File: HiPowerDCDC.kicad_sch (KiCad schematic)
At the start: 67 parts, among them J1 Conn_01x01, J2 Conn_01x01, J3 Conn_01x01, J4 Conn_01x01, J5 Conn_01x04, Q1 WMJ38N60, Q2 WMJ38N60, SW1 SW_Push, SW2 SW_Push, U1 ESP32-WROOM-32U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

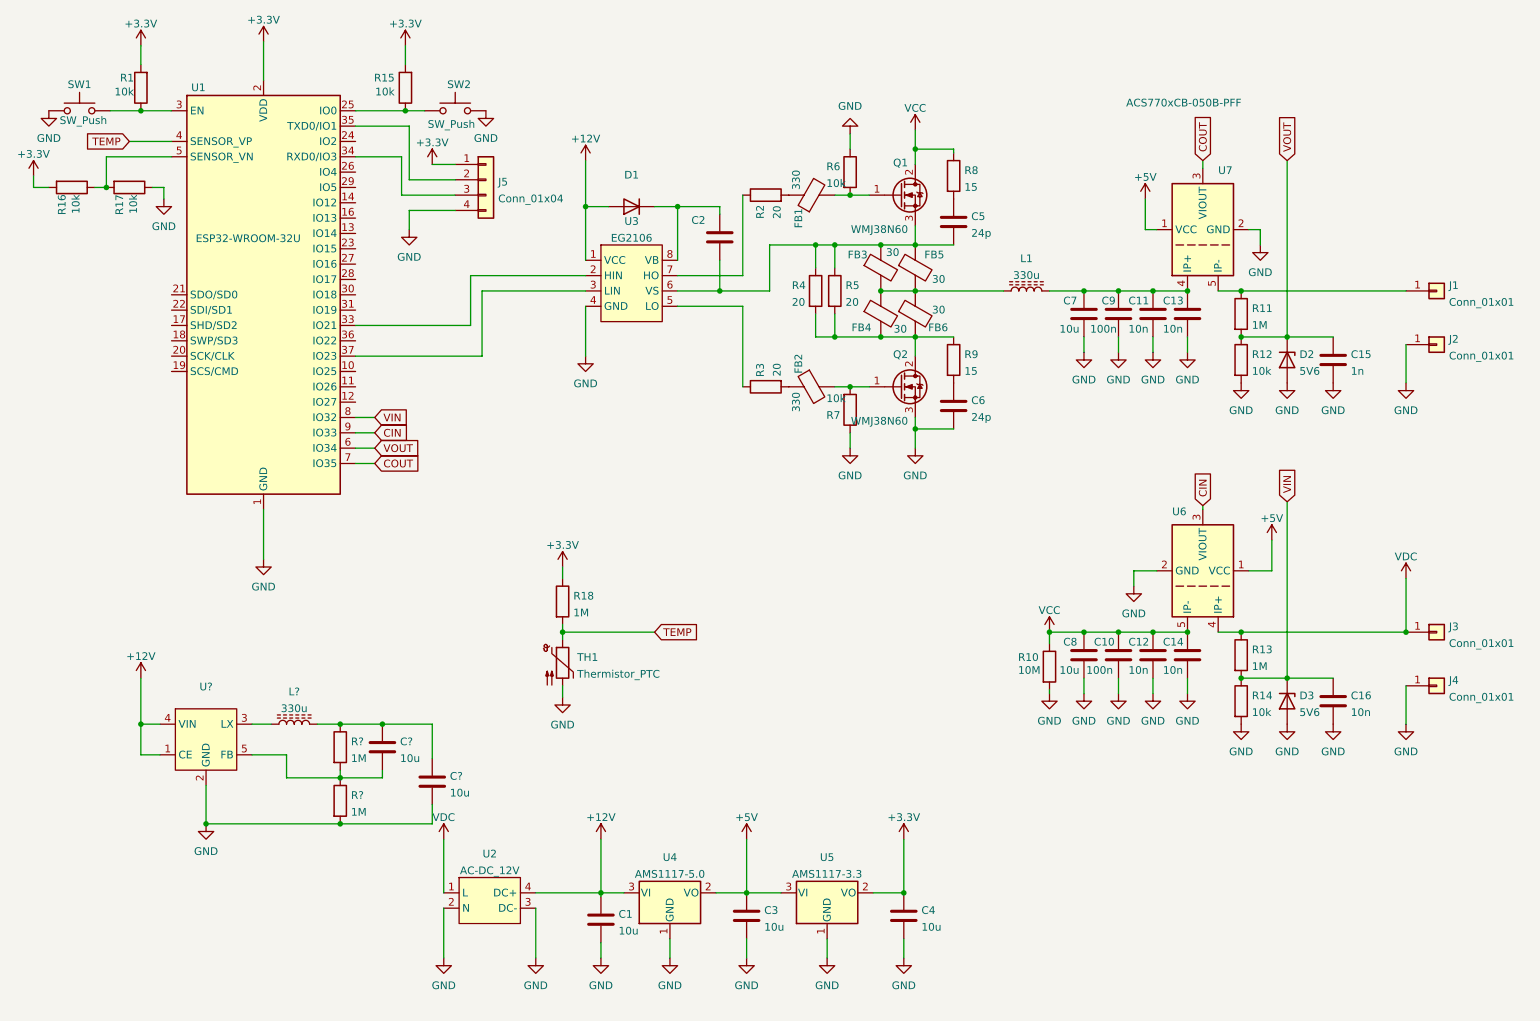
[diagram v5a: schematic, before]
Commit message: Added DCDC converter 12V->5V
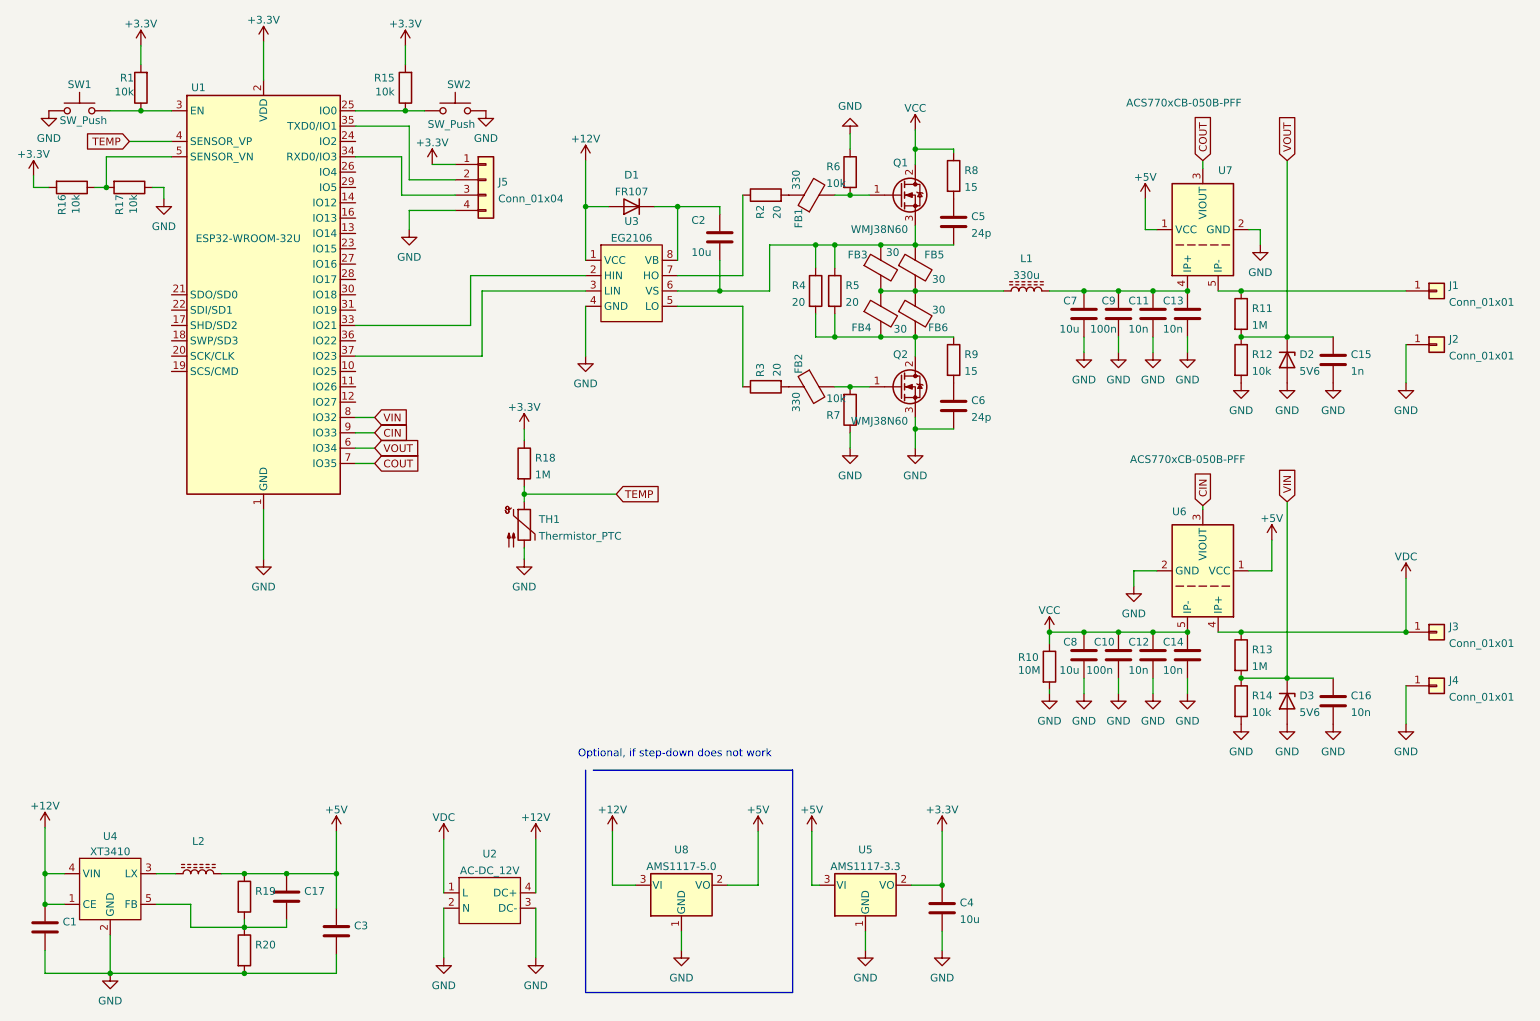
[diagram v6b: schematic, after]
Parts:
- removed C3: 10u, Capacitor_SMD:C_1206_3216Metric, symbol Device:C
- removed U4: AMS1117-5.0, Package_TO_SOT_SMD:SOT-223-3_TabPin2, symbol Regulator_Linear:AMS1117-5.0
- added U8: AMS1117-5.0, Package_TO_SOT_SMD:SOT-223-3_TabPin2, symbol Regulator_Linear:AMS1117-5.0
- C1: value 10u -> (none); footprint Capacitor_SMD:C_1206_3216Metric -> (none)
- C17, C3: renamed from C?; value 10u -> (none); footprint Capacitor_SMD:C_1206_3216Metric -> (none)
- C2: value (none) -> 10u; footprint (none) -> Capacitor_SMD:C_1206_3216Metric
- D1: value (none) -> FR107; footprint (none) -> Diode_SMD:D_SOD-123
- L2: renamed from L?; value 330u -> (none); footprint Inductor_THT:L_Toroid_Vertical_L54.0mm_W23.8mm_P20.10mm_Bourns_5700 -> (none)
- R19, R20: renamed from R?; value 1M -> (none); footprint Resistor_SMD:R_1206_3216Metric -> (none)
- U4: renamed from U?; value (none) -> XT3410
- U6: value (none) -> ACS770xCB-050B-PFF; footprint (none) -> Sensor_Current:Allegro_CB_PFF
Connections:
- net +12V: now also U8.3 (VI)
- net +5V: now also C17.1, C3.1, L2.2, R19.1, U8.2 (VO)
- net GND: now also U8.1 (GND)
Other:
- note added: "Optional, if step-down does not work"
- moved on the sheet: C17, C3, C4, L2, R18, R19, R20, TH1, U4, U5

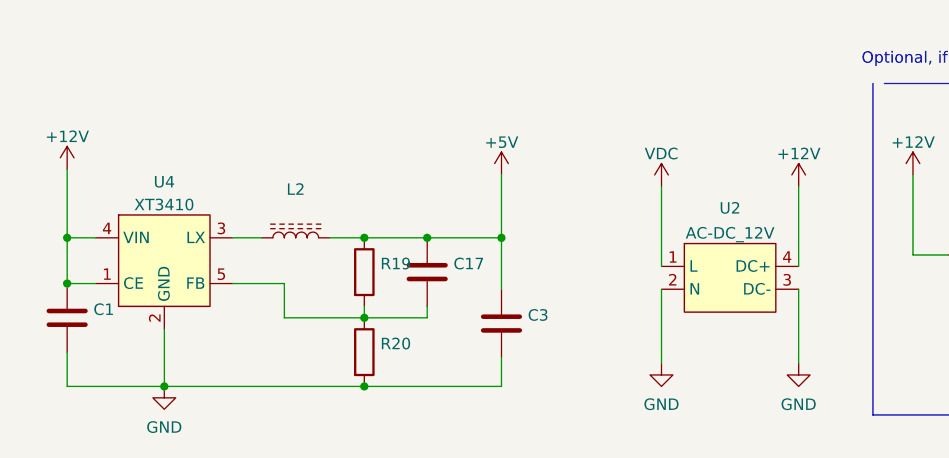
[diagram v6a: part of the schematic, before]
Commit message: Changed ACDC converter to HLK-PM12
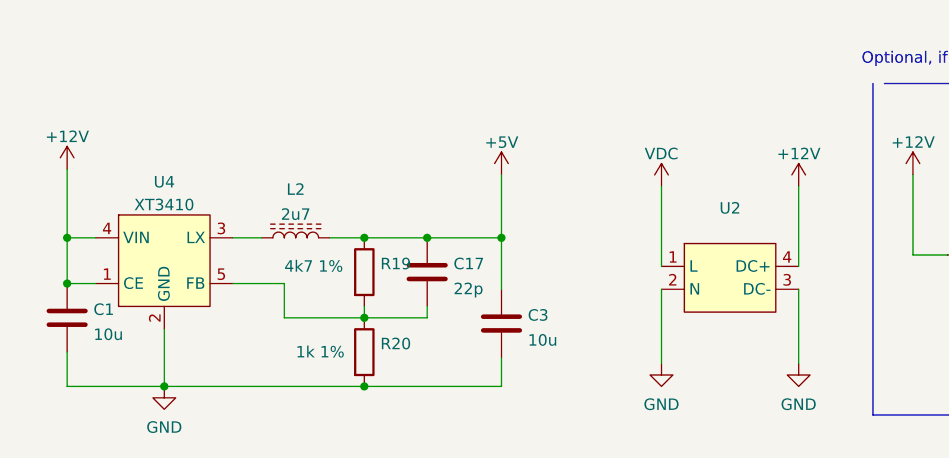
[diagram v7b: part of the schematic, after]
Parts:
- C1, C3: value (none) -> 10u; footprint (none) -> Capacitor_SMD:C_1206_3216Metric
- C17: value (none) -> 22p; footprint (none) -> Capacitor_SMD:C_1206_3216Metric
- L2: value (none) -> 2u7; footprint (none) -> Inductor_SMD:L_1206_3216Metric
- R19: value (none) -> 4k7 1%; footprint (none) -> Resistor_SMD:R_1206_3216Metric
- R20: value (none) -> 1k 1%; footprint (none) -> Resistor_SMD:R_1206_3216Metric
- U2: value AC-DC_12V -> (none); footprint HiPowerFP:AC_DC_PCB_straight -> (none)
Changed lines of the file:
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@@
       (effects (font (size 1.27 1.27)) (justify left))
     )
-    (property "Value" "" (id 1) (at 62.6111 177.7616 0)
-      (effects (font (size 1.27 1.27)) (justify left))
-    )
-    (property "Footprint" "" (id 2) (at 60.6552 179.705 0)
+    (property "Value" "22p" (id 1) (at 62.6111 177.7616 0)
+      (effects (font (size 1.27 1.27)) (justify left))
+    )
+    (property "Footprint" "Capacitor_SMD:C_1206_3216Metric" (id 2) (at 60.6552 179.705 0)
       (effects (font (size 1.27 1.27)) hide)
     )
@@
       (effects (font (size 1.27 1.27)) (justify left))
     )
-    (property "Value" "" (id 1) (at 70.8661 183.4766 0)
-      (effects (font (size 1.27 1.27)) (justify left))
-    )
-    (property "Footprint" "" (id 2) (at 68.9102 185.42 0)
+    (property "Value" "10u" (id 1) (at 70.8661 183.4766 0)
+      (effects (font (size 1.27 1.27)) (justify left))
+    )
+    (property "Footprint" "Capacitor_SMD:C_1206_3216Metric" (id 2) (at 68.9102 185.42 0)
       (effects (font (size 1.27 1.27)) hide)
     )
@@
       (effects (font (size 1.27 1.27)) (justify left))
     )
-    (property "Value" "" (id 1) (at 45.085 184.785 0)
-      (effects (font (size 1.27 1.27)) (justify left))
-    )
-    (property "Footprint" "" (id 2) (at 50.927 184.785 90)
+    (property "Value" "1k 1%" (id 1) (at 45.085 184.785 0)
+      (effects (font (size 1.27 1.27)) (justify left))
+    )
+    (property "Footprint" "Resistor_SMD:R_1206_3216Metric" (id 2) (at 50.927 184.785 90)
       (effects (font (size 1.27 1.27)) hide)
     )
@@
     (in_bom yes) (on_board yes) (fields_autoplaced)
     (property "Reference" "U2" (id 0) (at 93.345 168.8042 0))
-    (property "Value" "AC-DC_12V" (id 1) (at 93.345 171.5793 0))
-    (property "Footprint" "HiPowerFP:AC_DC_PCB_straight" (id 2) (at 93.345 180.34 0)
-      (effects (font (size 1.27 1.27)) hide)
-    )
-    (property "Datasheet" "" (id 3) (at 93.345 180.34 0)
+    (property "Value" "" (id 1) (at 93.345 171.5793 0))
+    (property "Footprint" "" (id 2) (at 93.345 180.34 0)
+      (effects (font (size 1.27 1.27)) hide)
+    )
+    (property "Datasheet" "https://datasheet.lcsc.com/szlcsc/1909111105_HI-LINK-HLK-PM24_C399250.pdf" (id 3) (at 93.345 180.34 0)
       (effects (font (size 1.27 1.27)) hide)
     )
@@
     (in_bom yes) (on_board yes) (fields_autoplaced)
     (property "Reference" "L2" (id 0) (at 45.085 166.7214 90))
-    (property "Value" "" (id 1) (at 45.085 169.4965 90))
-    (property "Footprint" "" (id 2) (at 45.085 172.085 0)
+    (property "Value" "2u7" (id 1) (at 45.085 169.4965 90))
+    (property "Footprint" "Inductor_SMD:L_1206_3216Metric" (id 2) (at 45.085 172.085 0)
       (effects (font (size 1.27 1.27)) hide)
     )
@@
       (effects (font (size 1.27 1.27)) (justify left))
     )
-    (property "Value" "" (id 1) (at 22.6061 182.8416 0)
-      (effects (font (size 1.27 1.27)) (justify left))
-    )
-    (property "Footprint" "" (id 2) (at 20.6502 184.785 0)
+    (property "Value" "10u" (id 1) (at 22.6061 182.8416 0)
+      (effects (font (size 1.27 1.27)) (justify left))
+    )
+    (property "Footprint" "Capacitor_SMD:C_1206_3216Metric" (id 2) (at 20.6502 184.785 0)
       (effects (font (size 1.27 1.27)) hide)
     )
@@
       (effects (font (size 1.27 1.27)) (justify left))
     )
-    (property "Value" "" (id 1) (at 43.815 175.26 0)
-      (effects (font (size 1.27 1.27)) (justify left))
-    )
-    (property "Footprint" "" (id 2) (at 50.927 175.895 90)
+    (property "Value" "4k7 1%" (id 1) (at 43.815 175.26 0)
+      (effects (font (size 1.27 1.27)) (justify left))
+    )
+    (property "Footprint" "Resistor_SMD:R_1206_3216Metric" (id 2) (at 50.927 175.895 90)
       (effects (font (size 1.27 1.27)) hide)
     )
@@
     )
     (path "/6c2dea70-da55-46ab-bd1c-a38f173c0bc4"
-      (reference "U2") (unit 1) (value "AC-DC_12V") (footprint "HiPowerFP:AC_DC_PCB_straight")
+      (reference "U2") (unit 1) (value "AC-DC_12V") (footprint "HiPowerFP:HLK-PM12")
     )
     (path "/9525c9c1-5ac2-436c-a8e0-b3326779d385"

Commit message: Finished PCB
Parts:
- L1: value 330u -> (none); footprint Inductor_THT:L_Toroid_Vertical_L54.0mm_W23.8mm_P20.10mm_Bourns_5700 -> (none)
- U2: value (none) -> AC-DC_12V; footprint (none) -> HiPowerFP:HLK-PM12
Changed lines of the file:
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@@
     (in_bom yes) (on_board yes) (fields_autoplaced)
     (property "Reference" "L1" (id 0) (at 182.245 70.2014 90))
-    (property "Value" "330u" (id 1) (at 182.245 72.9765 90))
-    (property "Footprint" "Inductor_THT:L_Toroid_Vertical_L54.0mm_W23.8mm_P20.10mm_Bourns_5700" (id 2) (at 182.245 75.565 0)
+    (property "Value" "" (id 1) (at 182.245 72.9765 90))
+    (property "Footprint" "" (id 2) (at 182.245 75.565 0)
       (effects (font (size 1.27 1.27)) hide)
     )
@@
     (in_bom yes) (on_board yes) (fields_autoplaced)
     (property "Reference" "U2" (id 0) (at 93.345 168.8042 0))
-    (property "Value" "" (id 1) (at 93.345 171.5793 0))
-    (property "Footprint" "" (id 2) (at 93.345 180.34 0)
+    (property "Value" "AC-DC_12V" (id 1) (at 93.345 171.5793 0))
+    (property "Footprint" "HiPowerFP:HLK-PM12" (id 2) (at 93.345 180.34 0)
       (effects (font (size 1.27 1.27)) hide)
     )
@@
     )
     (path "/207aa92c-0a58-42a5-a198-d707640ce308"
-      (reference "L1") (unit 1) (value "330u") (footprint "Inductor_THT:L_Toroid_Vertical_L54.0mm_W23.8mm_P20.10mm_Bourns_5700")
+      (reference "L1") (unit 1) (value "330u") (footprint "HiPowerFP:L_Toroid_Vertical_L54.0mm_W23.8mm_P20.10mm_Bourns_5700")
     )
     (path "/95159484-e5f5-4966-8d7a-72189e5ff978"
